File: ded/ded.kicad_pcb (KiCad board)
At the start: 2 copper layers, 13 x 13.7 mm, 4 parts

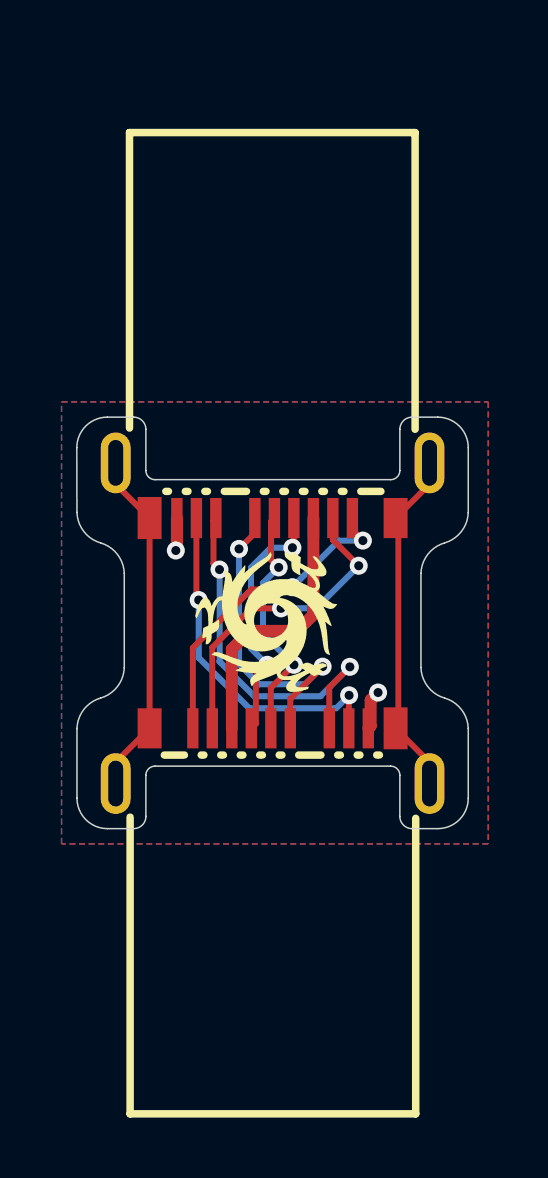
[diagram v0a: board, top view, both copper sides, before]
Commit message: ded revision: new usb part, better trace/via routing for stability, better stiffener plan
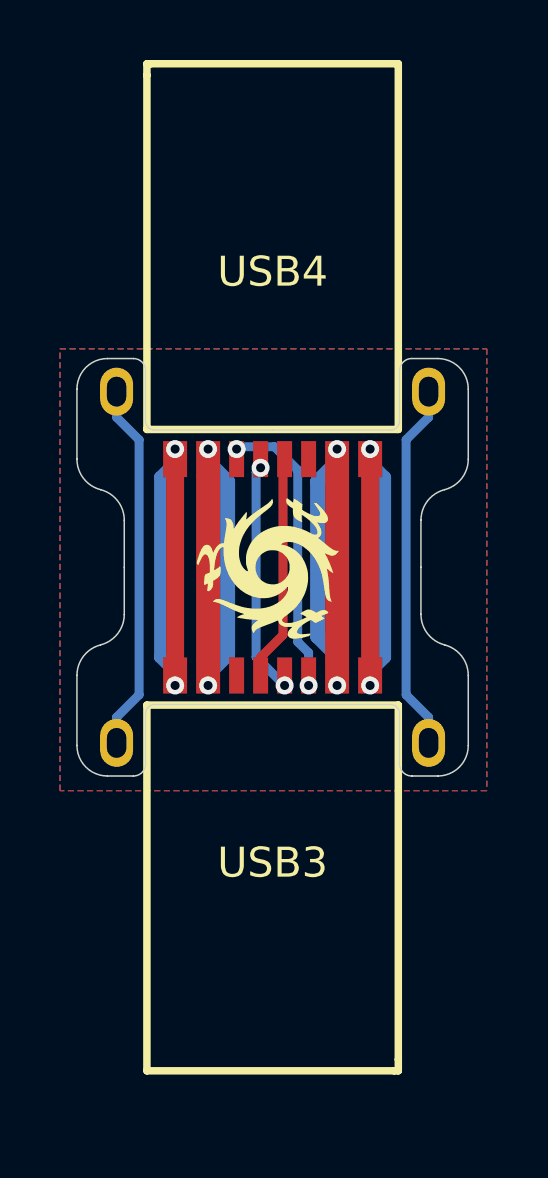
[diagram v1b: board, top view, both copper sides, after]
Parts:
- removed USB1, USB2: GT-USB-8016A, ded:USB-TYPE-C-SMD_GT-USB-8016A
- added USB3: HYCW675-USBC12-105B, ded:USB-C-SMD_HYCW675-USBC12-105B, F.Cu at (100.0, 104.7)
- added USB4: HYCW675-USBC12-105B, ded:USB-C-SMD_HYCW675-USBC12-105B, F.Cu at (100.0, 95.3)
- moved G*** 1.77 mm to (100.0, 100.0)
- moved G*** 1.75 mm to (100.0, 100.0)
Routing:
- net /VBUS: track 0.00 -> 28.9 mm, vias 0 -> 4
- net /GND: track 0.00 -> 28.6 mm, vias 0 -> 4
- net /SHIELD: track 0.00 -> 24.7 mm
- net Net-(USB1-Shield): track 23.3 -> 0.00 mm
- net Net-(USB1-TX1-): track 12.5 -> 0.00 mm, vias 2 -> 0
- net Net-(USB1-TX1+): track 11.7 -> 0.00 mm, vias 2 -> 0
- net Net-(USB1-CC1): track 10.9 -> 0.00 mm, vias 2 -> 0
- net Net-(USB1-RX1-): track 10.7 -> 0.00 mm, vias 2 -> 0
- net Net-(USB1-RX1+): track 10.7 -> 0.00 mm, vias 2 -> 0
- net /CC: track 0.00 -> 9.72 mm, vias 0 -> 2
- net VBUS: track 9.06 -> 0.00 mm
- net Net-(USB1-D-): track 8.47 -> 0.00 mm, vias 2 -> 0
- net Net-(USB1-D+): track 8.12 -> 0.00 mm, vias 2 -> 0
- net /USB2_D+: track 0.00 -> 8.00 mm, vias 0 -> 2
- net /USB2_D-: track 0.00 -> 7.54 mm
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- added copper zone on B.Cu, net /GND
- added copper zone on F.Cu, net /GND
- removed copper zone on B.Cu, net GND
- removed copper zone on F.Cu, net VBUS
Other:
- board size 13 x 13.7 mm -> 13 x 13.9 mm
- board text added: "stiffener (User.2): FR-4 0.6mm bottom"
- board text removed: "Stiffener: Stainless Steel Location: Stiffener layer (back side) Thickness: 0.2mm"

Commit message: coupler usb part change
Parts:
- USB3, USB4: value HYCW675-USBC12-105B -> HYCW676-USBC12-105B
